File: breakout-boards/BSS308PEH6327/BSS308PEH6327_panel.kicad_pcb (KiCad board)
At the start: 2 copper layers, 93.5 x 68.7 mm, 68 parts, among them J1 Conn_01x12, J2 Conn_01x12, J3 Conn_01x12, Q1 BSS308PE_H6327, Q10 BSS308PE_H6327, Q11 BSS308PE_H6327, Q12 BSS308PE_H6327, Q2 BSS308PE_H6327, Q3 BSS308PE_H6327, Q4 BSS308PE_H6327, Q5 BSS308PE_H6327, Q6 BSS308PE_H6327, Q7 BSS308PE_H6327, Q8 BSS308PE_H6327, Q9 BSS308PE_H6327

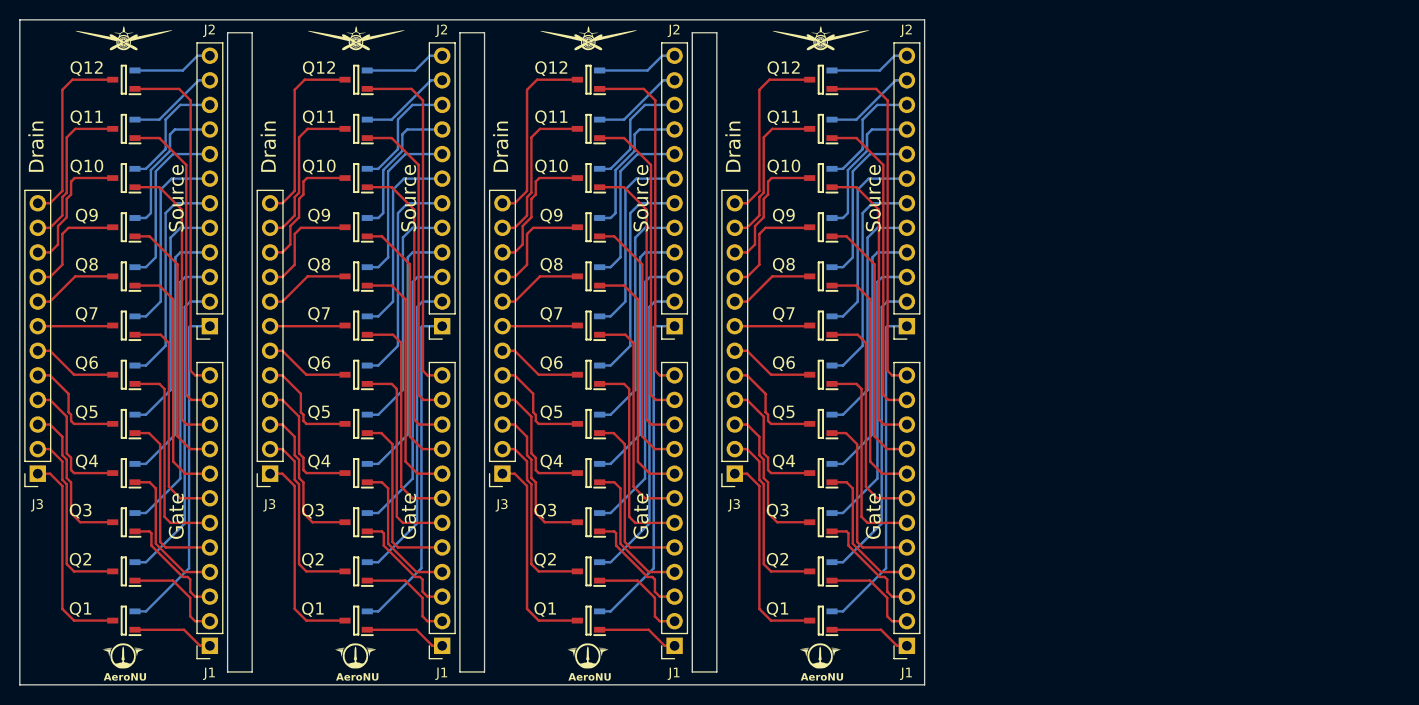
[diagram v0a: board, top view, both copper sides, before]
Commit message: feat: change fixed wing logo and component positioning
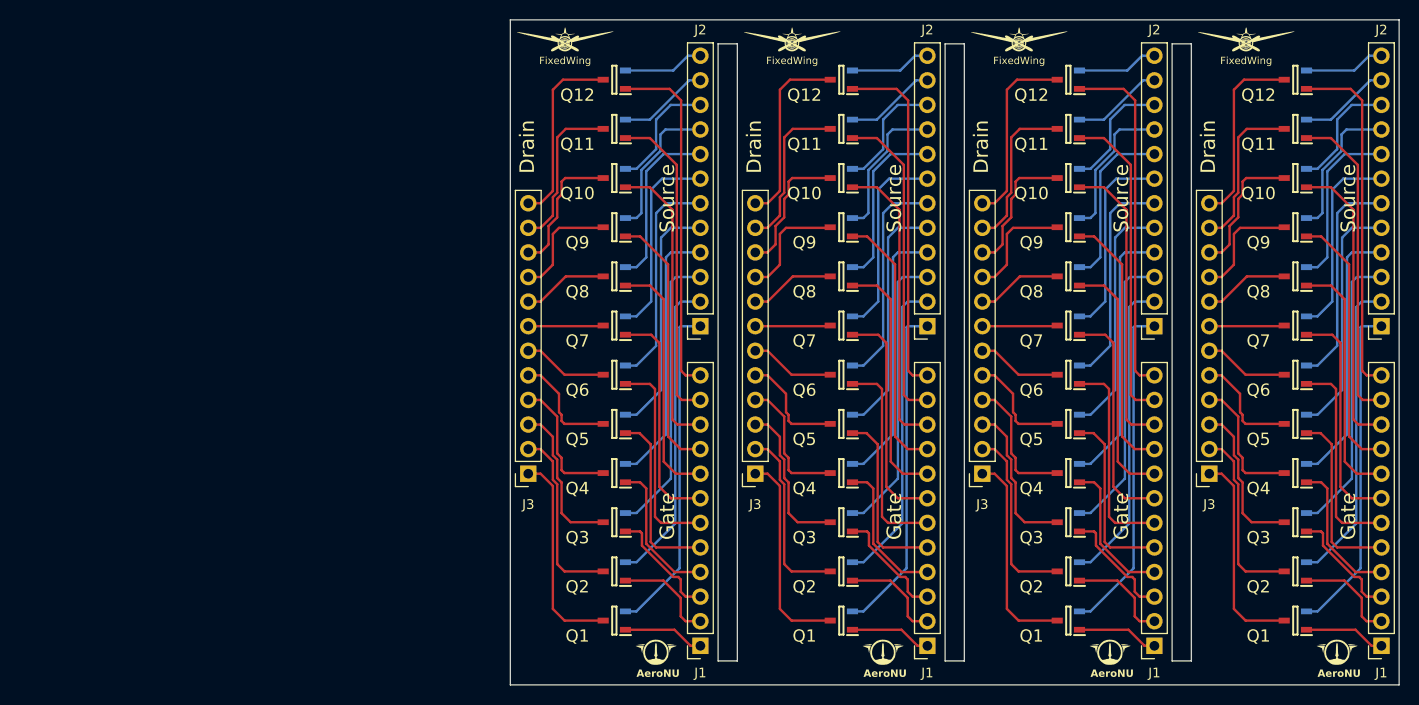
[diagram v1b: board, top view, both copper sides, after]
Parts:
- removed the AeroNU at (158.7, 125.7)
- removed the AeroNU at (134.7, 125.7)
- removed the AeroNU at (182.7, 125.7)
- removed the FixedWing at (110.6, 59.8)
- removed the FixedWing at (134.6, 59.8)
- removed the FixedWing at (182.6, 59.8)
- removed the FixedWing at (158.6, 59.8)
- removed the J1 at (167.5, 121.9)
- removed the J1 at (143.5, 121.9)
- removed the J1 at (191.5, 121.9)
- removed the J2 at (167.5, 88.9)
- removed the J2 at (143.5, 88.9)
- removed the J2 at (191.5, 88.9)
- removed the J3 at (149.7, 104.1)
- removed the J3 at (125.7, 104.1)
- removed the J3 at (173.7, 104.1)
- removed the Q1 at (182.6, 119.3)
- removed the Q1 at (158.6, 119.3)
- removed the Q1 at (134.6, 119.3)
- removed the Q10 at (182.6, 73.6)
- removed the Q10 at (134.6, 73.6)
- removed the Q10 at (158.6, 73.6)
- removed the Q11 at (182.6, 68.5)
- removed the Q11 at (158.6, 68.5)
- removed the Q11 at (134.6, 68.5)
- removed the Q12 at (158.6, 63.4)
- removed the Q12 at (134.6, 63.4)
- removed the Q12 at (182.6, 63.4)
- removed the Q2 at (158.6, 114.2)
- removed the Q2 at (134.6, 114.2)
- removed the Q2 at (182.6, 114.2)
- removed the Q3 at (134.6, 109.2)
- removed the Q3 at (182.6, 109.2)
- removed the Q3 at (158.6, 109.2)
- removed the Q4 at (134.6, 104.1)
- removed the Q4 at (182.6, 104.1)
- removed the Q4 at (158.6, 104.1)
- removed the Q5 at (182.6, 99.0)
- removed the Q5 at (134.6, 99.0)
- removed the Q5 at (158.6, 99.0)
- removed the Q6 at (134.6, 93.9)
- removed the Q6 at (158.6, 93.9)
- removed the Q6 at (182.6, 93.9)
- removed the Q7 at (158.6, 88.8)
- removed the Q7 at (182.6, 88.8)
- removed the Q7 at (134.6, 88.8)
- removed the Q8 at (134.6, 83.8)
- removed the Q8 at (158.6, 83.8)
- removed the Q8 at (182.6, 83.8)
- removed the Q9 at (182.6, 78.7)
- removed the Q9 at (158.6, 78.7)
- removed the Q9 at (134.6, 78.7)
- added AeroNU: LOGO, FixedWing:AeroNU - Logo (Smol), F.Cu at (189.2, 125.4)
- added AeroNU: LOGO, FixedWing:AeroNU - Logo (Smol), F.Cu at (212.6, 125.4)
- added AeroNU: LOGO, FixedWing:AeroNU - Logo (Smol), F.Cu at (236.1, 125.4)
- added FixedWing: LOGO, FixedWing:FixedWing - Logo (Smol), F.Cu at (179.7, 59.7)
- added FixedWing: LOGO, FixedWing:FixedWing - Logo (Smol), F.Cu at (203.1, 59.7)
- added FixedWing: LOGO, FixedWing:FixedWing - Logo (Smol), F.Cu at (226.6, 59.7)
- added FixedWing: LOGO, FixedWing:FixedWing - Logo (Smol), F.Cu at (156.2, 59.7)
- added J1: Conn_01x12, Connector_PinSocket_2.54mm:PinSocket_1x12_P2.54mm_Vertical, F.Cu at (193.6, 121.9)
- added J1: Conn_01x12, Connector_PinSocket_2.54mm:PinSocket_1x12_P2.54mm_Vertical, F.Cu at (240.5, 121.9)
- added J1: Conn_01x12, Connector_PinSocket_2.54mm:PinSocket_1x12_P2.54mm_Vertical, F.Cu at (217.1, 121.9)
- added J2: Conn_01x12, Connector_PinSocket_2.54mm:PinSocket_1x12_P2.54mm_Vertical, F.Cu at (217.1, 88.9)
- added J2: Conn_01x12, Connector_PinSocket_2.54mm:PinSocket_1x12_P2.54mm_Vertical, F.Cu at (240.5, 88.9)
- added J2: Conn_01x12, Connector_PinSocket_2.54mm:PinSocket_1x12_P2.54mm_Vertical, F.Cu at (193.6, 88.9)
- added J3: Conn_01x12, Connector_PinSocket_2.54mm:PinSocket_1x12_P2.54mm_Vertical, F.Cu at (222.8, 104.1)
- added J3: Conn_01x12, Connector_PinSocket_2.54mm:PinSocket_1x12_P2.54mm_Vertical, F.Cu at (199.3, 104.1)
- added J3: Conn_01x12, Connector_PinSocket_2.54mm:PinSocket_1x12_P2.54mm_Vertical, F.Cu at (175.9, 104.1)
- added Q1: BSS308PE_H6327, FixedWing:SOT95P260X110-3N, F.Cu at (184.7, 119.3)
- added Q1: BSS308PE_H6327, FixedWing:SOT95P260X110-3N, F.Cu at (208.2, 119.3)
- added Q1: BSS308PE_H6327, FixedWing:SOT95P260X110-3N, F.Cu at (231.6, 119.3)
- added Q10: BSS308PE_H6327, FixedWing:SOT95P260X110-3N, F.Cu at (184.7, 73.6)
- added Q10: BSS308PE_H6327, FixedWing:SOT95P260X110-3N, F.Cu at (208.2, 73.6)
- added Q10: BSS308PE_H6327, FixedWing:SOT95P260X110-3N, F.Cu at (231.6, 73.6)
- added Q11: BSS308PE_H6327, FixedWing:SOT95P260X110-3N, F.Cu at (231.6, 68.5)
- added Q11: BSS308PE_H6327, FixedWing:SOT95P260X110-3N, F.Cu at (184.7, 68.5)
- added Q11: BSS308PE_H6327, FixedWing:SOT95P260X110-3N, F.Cu at (208.2, 68.5)
- added Q12: BSS308PE_H6327, FixedWing:SOT95P260X110-3N, F.Cu at (208.2, 63.4)
- added Q12: BSS308PE_H6327, FixedWing:SOT95P260X110-3N, F.Cu at (231.6, 63.4)
- added Q12: BSS308PE_H6327, FixedWing:SOT95P260X110-3N, F.Cu at (184.7, 63.4)
- added Q2: BSS308PE_H6327, FixedWing:SOT95P260X110-3N, F.Cu at (184.7, 114.2)
- added Q2: BSS308PE_H6327, FixedWing:SOT95P260X110-3N, F.Cu at (231.6, 114.2)
- added Q2: BSS308PE_H6327, FixedWing:SOT95P260X110-3N, F.Cu at (208.2, 114.2)
- added Q3: BSS308PE_H6327, FixedWing:SOT95P260X110-3N, F.Cu at (184.7, 109.2)
- added Q3: BSS308PE_H6327, FixedWing:SOT95P260X110-3N, F.Cu at (208.2, 109.2)
- added Q3: BSS308PE_H6327, FixedWing:SOT95P260X110-3N, F.Cu at (231.6, 109.2)
- added Q4: BSS308PE_H6327, FixedWing:SOT95P260X110-3N, F.Cu at (208.2, 104.1)
- added Q4: BSS308PE_H6327, FixedWing:SOT95P260X110-3N, F.Cu at (231.6, 104.1)
- added Q4: BSS308PE_H6327, FixedWing:SOT95P260X110-3N, F.Cu at (184.7, 104.1)
- added Q5: BSS308PE_H6327, FixedWing:SOT95P260X110-3N, F.Cu at (231.6, 99.0)
- added Q5: BSS308PE_H6327, FixedWing:SOT95P260X110-3N, F.Cu at (184.7, 99.0)
- added Q5: BSS308PE_H6327, FixedWing:SOT95P260X110-3N, F.Cu at (208.2, 99.0)
- added Q6: BSS308PE_H6327, FixedWing:SOT95P260X110-3N, F.Cu at (184.7, 93.9)
- added Q6: BSS308PE_H6327, FixedWing:SOT95P260X110-3N, F.Cu at (208.2, 93.9)
- added Q6: BSS308PE_H6327, FixedWing:SOT95P260X110-3N, F.Cu at (231.6, 93.9)
- added Q7: BSS308PE_H6327, FixedWing:SOT95P260X110-3N, F.Cu at (208.2, 88.8)
- added Q7: BSS308PE_H6327, FixedWing:SOT95P260X110-3N, F.Cu at (184.7, 88.8)
- added Q7: BSS308PE_H6327, FixedWing:SOT95P260X110-3N, F.Cu at (231.6, 88.8)
- added Q8: BSS308PE_H6327, FixedWing:SOT95P260X110-3N, F.Cu at (184.7, 83.8)
- added Q8: BSS308PE_H6327, FixedWing:SOT95P260X110-3N, F.Cu at (231.6, 83.8)
- added Q8: BSS308PE_H6327, FixedWing:SOT95P260X110-3N, F.Cu at (208.2, 83.8)
- added Q9: BSS308PE_H6327, FixedWing:SOT95P260X110-3N, F.Cu at (208.2, 78.7)
- added Q9: BSS308PE_H6327, FixedWing:SOT95P260X110-3N, F.Cu at (231.6, 78.7)
- added Q9: BSS308PE_H6327, FixedWing:SOT95P260X110-3N, F.Cu at (184.7, 78.7)
- moved AeroNU 55.0 mm to (165.7, 125.4)
- moved J1 50.7 mm to (170.2, 121.9)
- moved J2 50.7 mm to (170.2, 88.9)
- moved J3 50.7 mm to (152.4, 104.1)
- moved Q1 50.7 mm to (161.3, 119.3)
- moved Q10 50.7 mm to (161.3, 73.6)
- moved Q11 50.7 mm to (161.3, 68.5)
- moved Q12 50.7 mm to (161.3, 63.4)
- moved Q2 50.7 mm to (161.3, 114.2)
- moved Q3 50.7 mm to (161.3, 109.2)
- moved Q4 50.7 mm to (161.3, 104.1)
- moved Q5 50.7 mm to (161.3, 99.0)
- moved Q6 50.7 mm to (161.3, 93.9)
- moved Q7 50.7 mm to (161.3, 88.8)
- moved Q8 50.7 mm to (161.3, 83.8)
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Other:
- board size 93.5 x 68.7 mm -> 91.8 x 68.7 mm
